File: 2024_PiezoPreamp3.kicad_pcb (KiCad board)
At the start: 4 copper layers, 71 x 36.8 mm, 90 parts, among them J101 6.3mm stereo, J102 6.3mm stereo, J201 DC IN 5.5/2.1mm, J401 Spring Contact, U101 OPA145, U102 OPA145, U201 ZXMP3A17E6TA, U301 BC847BS,115

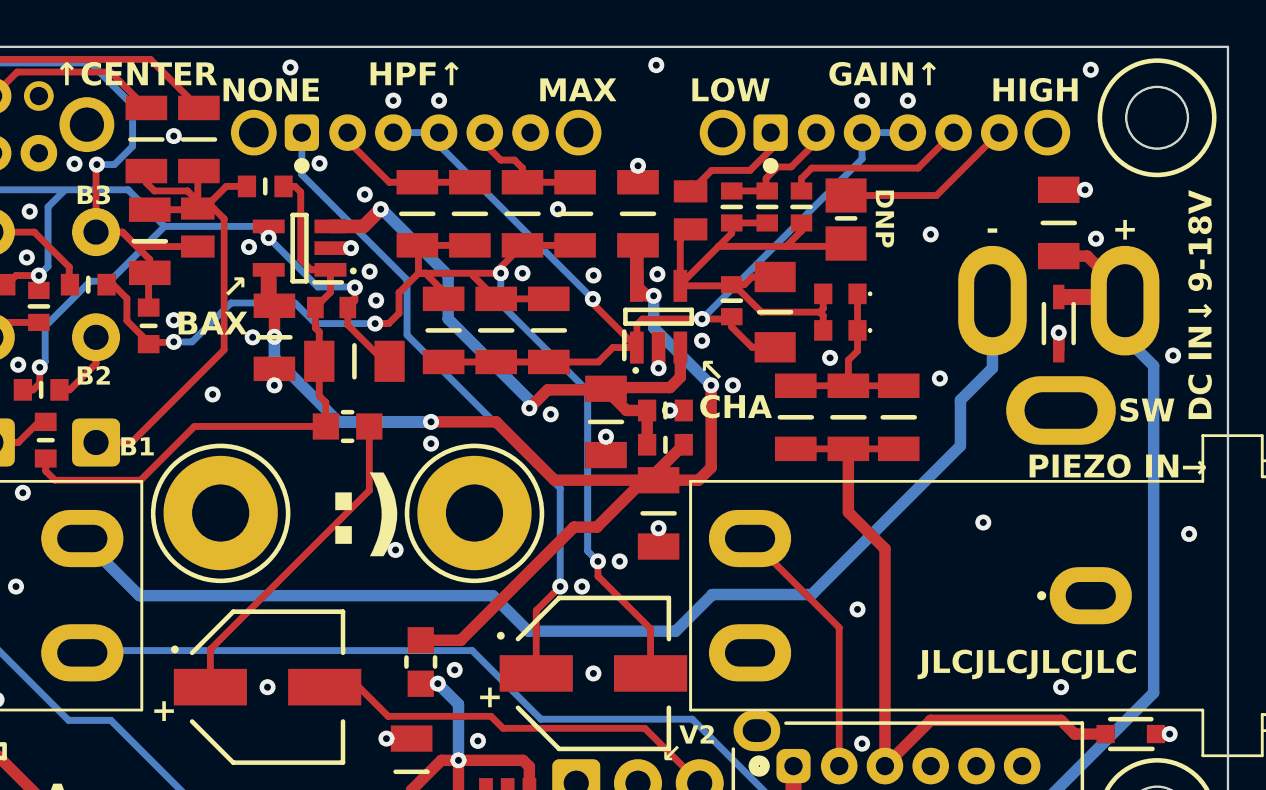
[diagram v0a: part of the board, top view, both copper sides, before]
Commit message: PCB: adding free holes for battery jack cables. Moving things around a bit
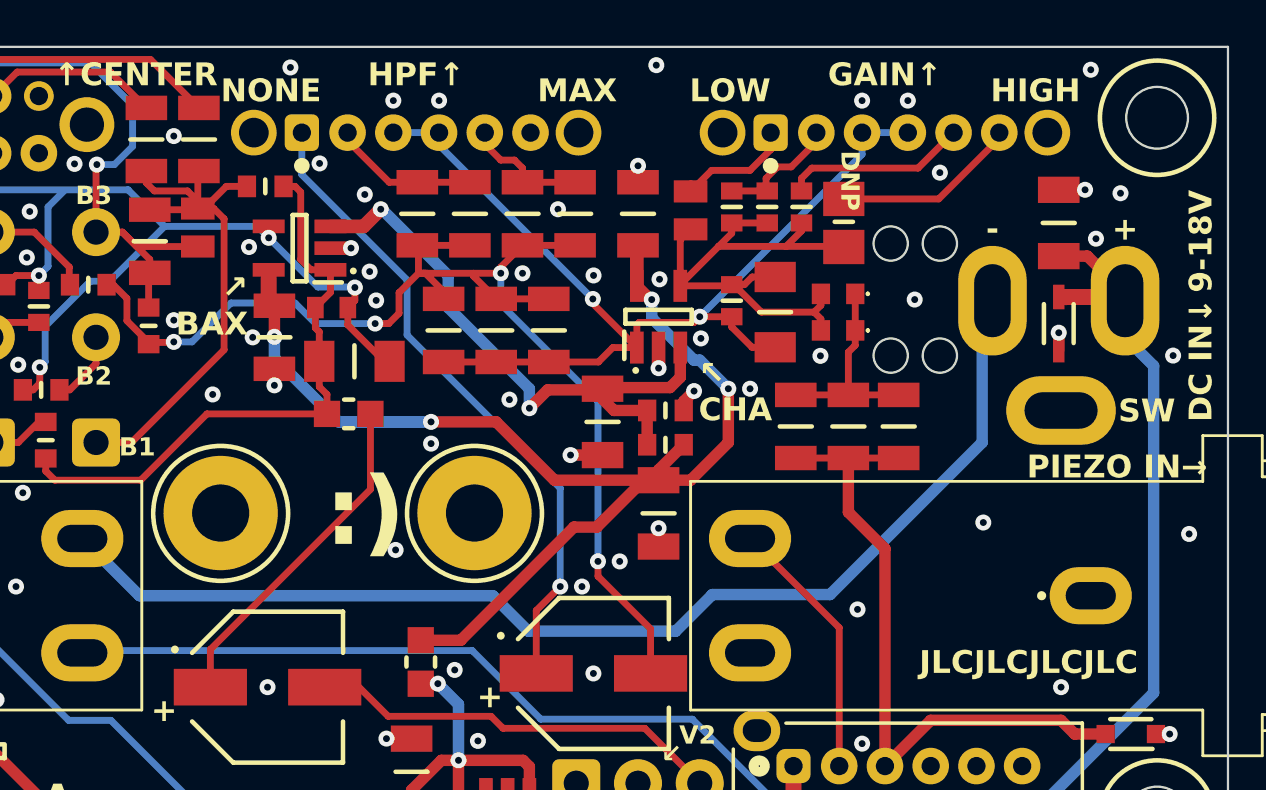
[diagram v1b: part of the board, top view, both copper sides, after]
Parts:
- added Batt1: FreeHole_1.5mm, library:FreeHole_1.5mm, F.Cu at (171.2, 83.7)
- added Batt2: FreeHole_1.5mm, library:FreeHole_1.5mm, F.Cu at (173.3, 83.7)
- added Batt3: FreeHole_1.5mm, library:FreeHole_1.5mm, F.Cu at (171.2, 88.5)
- added Batt4: FreeHole_1.5mm, library:FreeHole_1.5mm, F.Cu at (173.3, 88.5)
- moved R105 0.55 mm to (147.4, 91.1)
- moved C101 0.40 mm to (169.3, 91.7)
- moved C102 0.40 mm to (171.5, 91.7)
- moved C103 0.40 mm to (167.0, 91.7)
- moved Cf106 0.18 mm to (169.1, 82.7)
- moved C204 0.15 mm to (158.6, 91.5)
- moved R101 0.10 mm to (168.8, 85.8)
- moved R102 0.10 mm to (168.8, 87.5)
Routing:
- net GND: track 15.2 -> 16.2 mm, vias 85 -> 86
- net /1-ChargeAmpAndEQ/ROUT_COUT: track 14.3 -> 14.8 mm

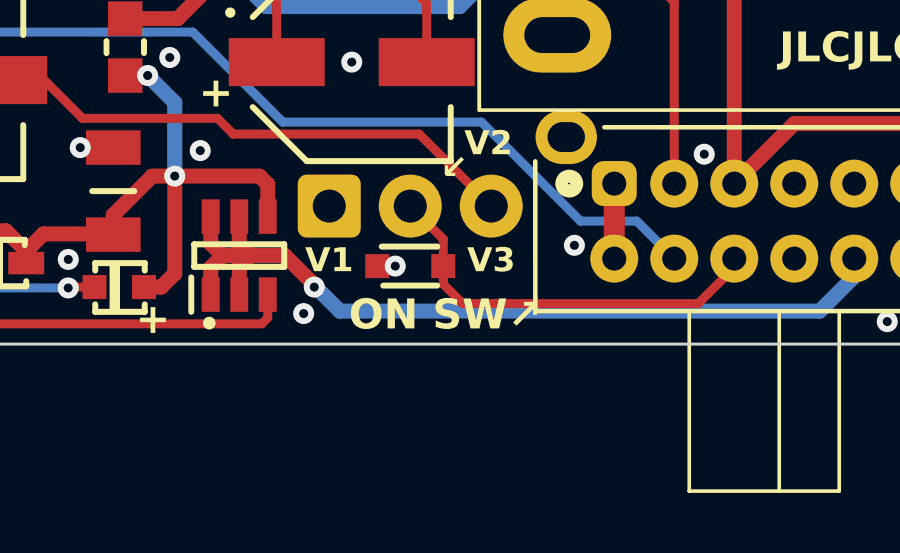
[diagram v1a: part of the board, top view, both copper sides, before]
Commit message: PCB: adjusting silkscreen, do not tent vias
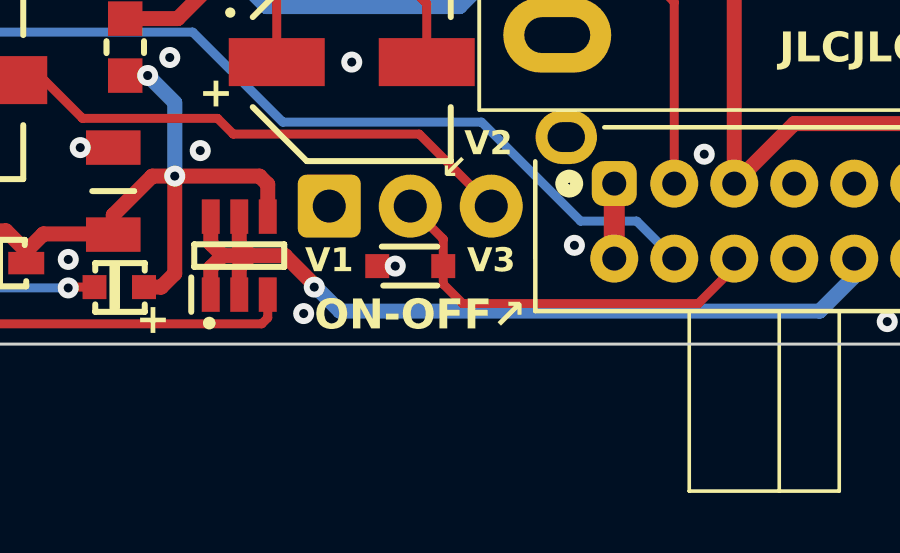
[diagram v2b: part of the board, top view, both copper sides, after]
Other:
- board text added: "ON-OFF↗"
- board text added: "↖ON/OFF"
- board text removed: "ON SW↗"
- board text removed: "←ON/OFF SW"
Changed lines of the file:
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@@
 			(svgprecision 4)
 			(plotframeref no)
-			(viasonmask yes)
+			(viasonmask no)
 			(mode 1)
 			(useauxorigin no)
@@
 		(sheetname "1-ChargeAmpAndEQ")
 		(sheetfile "1-ChargeAmpAndEQ.kicad_sch")
-		(attr through_hole exclude_from_bom)
+		(attr through_hole exclude_from_pos_files exclude_from_bom)
 		(pad "1" thru_hole circle
 			(at 0 0 90)
@@
 			)
 		)
-		(attr through_hole exclude_from_bom)
+		(attr through_hole exclude_from_pos_files exclude_from_bom)
 		(pad "1" thru_hole roundrect
 			(at 0 0)
@@
 		(sheetname "1-ChargeAmpAndEQ")
 		(sheetfile "1-ChargeAmpAndEQ.kicad_sch")
-		(attr through_hole exclude_from_bom)
+		(attr through_hole exclude_from_pos_files exclude_from_bom)
 		(pad "1" thru_hole circle
 			(at 0 0)
@@
 			)
 		)
-		(attr through_hole exclude_from_bom)
+		(attr through_hole exclude_from_pos_files exclude_from_bom)
 		(pad "1" thru_hole roundrect
 			(at 0 0)
@@
 		(sheetname "1-ChargeAmpAndEQ")
 		(sheetfile "1-ChargeAmpAndEQ.kicad_sch")
-		(attr through_hole exclude_from_bom)
+		(attr through_hole exclude_from_pos_files exclude_from_bom)
 		(pad "1" thru_hole circle
 			(at 0 0 90)
@@
 			)
 		)
-		(attr through_hole exclude_from_bom)
+		(attr through_hole exclude_from_pos_files exclude_from_bom)
 		(pad "1" thru_hole roundrect
 			(at 0 0 90)
@@
 		(sheetname "1-ChargeAmpAndEQ")
 		(sheetfile "1-ChargeAmpAndEQ.kicad_sch")
-		(attr through_hole exclude_from_bom)
+		(attr through_hole exclude_from_pos_files exclude_from_bom)
 		(pad "1" thru_hole circle
 			(at 0 0)
@@
 		(sheetname "1-ChargeAmpAndEQ")
 		(sheetfile "1-ChargeAmpAndEQ.kicad_sch")
-		(attr through_hole exclude_from_bom)
+		(attr through_hole exclude_from_pos_files exclude_from_bom)
 		(pad "1" thru_hole circle
 			(at 0 0)
@@
 		(sheetname "1-ChargeAmpAndEQ")
 		(sheetfile "1-ChargeAmpAndEQ.kicad_sch")
-		(attr through_hole exclude_from_bom)
+		(attr through_hole exclude_from_pos_files exclude_from_bom)
 		(pad "1" thru_hole circle
 			(at 0 0)
@@
 		)
 	)
-	(gr_text "←ON/OFF SW"
-		(locked yes)
-		(at 155.5 110.25 0)
+	(gr_text "↖ON/OFF"
+		(at 158.4 111.05 0)
 		(layer "B.SilkS" knockout)
 		(effects
@@
 		)
 	)
-	(gr_text "ON SW↗"
-		(locked yes)
-		(at 158.05 111.45 0)
+	(gr_text "ON-OFF↗"
+		(at 156.9 111.45 0)
 		(layer "F.SilkS" knockout)
 		(effects
